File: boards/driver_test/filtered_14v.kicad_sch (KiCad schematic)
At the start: 3 parts

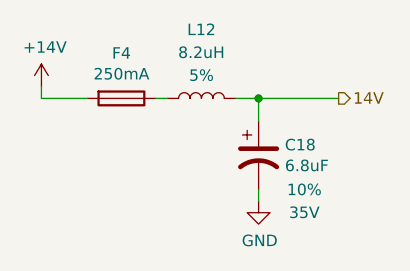
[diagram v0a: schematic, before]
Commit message: Driver: some high-level board rearrangement and addition of 3d models
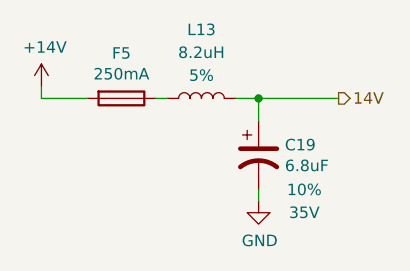
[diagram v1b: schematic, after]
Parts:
- renumbered C18 to C19, F4 to F5, L12 to L13
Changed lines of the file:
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@@
   (symbol (lib_id "Device:Fuse") (at 125.73 96.52 270)
     (in_bom yes) (on_board yes)
-    (property "Reference" "F4" (id 0) (at 125.73 91.5162 90))
+    (property "Reference" "F5" (id 0) (at 125.73 91.5162 90))
     (property "Value" "250mA" (id 1) (at 125.73 93.8276 90))
     (property "Footprint" "Fuse:Fuse_0603_1608Metric" (id 2) (at 125.73 94.742 90)
@@
   (symbol (lib_id "Device:L") (at 134.62 96.52 90)
     (in_bom yes) (on_board yes)
-    (property "Reference" "L12" (id 0) (at 134.62 88.9 90))
+    (property "Reference" "L13" (id 0) (at 134.62 88.9 90))
     (property "Value" "8.2uH" (id 1) (at 134.62 91.44 90))
     (property "Footprint" "Inductor_SMD:L_1812_4532Metric" (id 2) (at 134.62 96.52 0)
@@
   (symbol (lib_id "lachesis:+14V") (at 116.84 95.25 0)
     (in_bom yes) (on_board yes)
-    (property "Reference" "#PWR057" (id 0) (at 116.84 99.06 0)
+    (property "Reference" "#PWR061" (id 0) (at 116.84 99.06 0)
       (effects (font (size 1.27 1.27)) hide)
     )
@@
   (symbol (lib_id "power:GND") (at 140.97 107.95 0)
     (in_bom yes) (on_board yes)
-    (property "Reference" "#PWR058" (id 0) (at 140.97 114.3 0)
+    (property "Reference" "#PWR062" (id 0) (at 140.97 114.3 0)
       (effects (font (size 1.27 1.27)) hide)
     )
@@
   (symbol (lib_id "Device:C_Polarized_US") (at 140.97 102.87 0)
     (in_bom yes) (on_board yes)
-    (property "Reference" "C18" (id 0) (at 143.891 101.7016 0)
+    (property "Reference" "C19" (id 0) (at 143.891 101.7016 0)
       (effects (font (size 1.27 1.27)) (justify left))
     )

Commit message: Driver test: completed much of the preliminary layout.
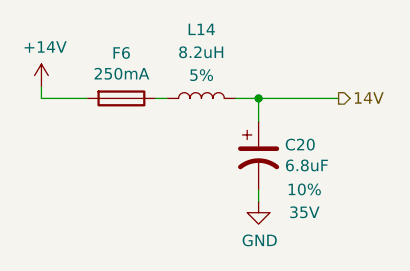
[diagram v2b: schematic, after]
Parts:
- renumbered C19 to C20, F5 to F6, L13 to L14
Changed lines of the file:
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@@
   (symbol (lib_id "Device:Fuse") (at 125.73 96.52 270)
     (in_bom yes) (on_board yes)
-    (property "Reference" "F5" (id 0) (at 125.73 91.5162 90))
+    (property "Reference" "F6" (id 0) (at 125.73 91.5162 90))
     (property "Value" "250mA" (id 1) (at 125.73 93.8276 90))
     (property "Footprint" "Fuse:Fuse_0603_1608Metric" (id 2) (at 125.73 94.742 90)
@@
   (symbol (lib_id "Device:L") (at 134.62 96.52 90)
     (in_bom yes) (on_board yes)
-    (property "Reference" "L13" (id 0) (at 134.62 88.9 90))
+    (property "Reference" "L14" (id 0) (at 134.62 88.9 90))
     (property "Value" "8.2uH" (id 1) (at 134.62 91.44 90))
     (property "Footprint" "Inductor_SMD:L_1812_4532Metric" (id 2) (at 134.62 96.52 0)
@@
   (symbol (lib_id "Device:C_Polarized_US") (at 140.97 102.87 0)
     (in_bom yes) (on_board yes)
-    (property "Reference" "C19" (id 0) (at 143.891 101.7016 0)
+    (property "Reference" "C20" (id 0) (at 143.891 101.7016 0)
       (effects (font (size 1.27 1.27)) (justify left))
     )

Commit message: Driver test: finished up board layout
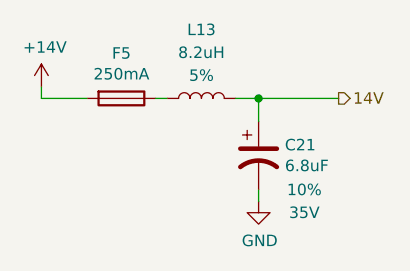
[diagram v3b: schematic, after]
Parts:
- renumbered C20 to C21, F6 to F5, L14 to L13
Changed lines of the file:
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@@
   (symbol (lib_id "Device:Fuse") (at 125.73 96.52 270)
     (in_bom yes) (on_board yes)
-    (property "Reference" "F6" (id 0) (at 125.73 91.5162 90))
+    (property "Reference" "F5" (id 0) (at 125.73 91.5162 90))
     (property "Value" "250mA" (id 1) (at 125.73 93.8276 90))
     (property "Footprint" "Fuse:Fuse_0603_1608Metric" (id 2) (at 125.73 94.742 90)
@@
   (symbol (lib_id "Device:L") (at 134.62 96.52 90)
     (in_bom yes) (on_board yes)
-    (property "Reference" "L14" (id 0) (at 134.62 88.9 90))
+    (property "Reference" "L13" (id 0) (at 134.62 88.9 90))
     (property "Value" "8.2uH" (id 1) (at 134.62 91.44 90))
     (property "Footprint" "Inductor_SMD:L_1812_4532Metric" (id 2) (at 134.62 96.52 0)
@@
   (symbol (lib_id "lachesis:+14V") (at 116.84 95.25 0)
     (in_bom yes) (on_board yes)
-    (property "Reference" "#PWR061" (id 0) (at 116.84 99.06 0)
+    (property "Reference" "#PWR065" (id 0) (at 116.84 99.06 0)
       (effects (font (size 1.27 1.27)) hide)
     )
@@
   (symbol (lib_id "power:GND") (at 140.97 107.95 0)
     (in_bom yes) (on_board yes)
-    (property "Reference" "#PWR062" (id 0) (at 140.97 114.3 0)
+    (property "Reference" "#PWR066" (id 0) (at 140.97 114.3 0)
       (effects (font (size 1.27 1.27)) hide)
     )
@@
   (symbol (lib_id "Device:C_Polarized_US") (at 140.97 102.87 0)
     (in_bom yes) (on_board yes)
-    (property "Reference" "C20" (id 0) (at 143.891 101.7016 0)
+    (property "Reference" "C21" (id 0) (at 143.891 101.7016 0)
       (effects (font (size 1.27 1.27)) (justify left))
     )

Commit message: Driver test: some minor component value changes
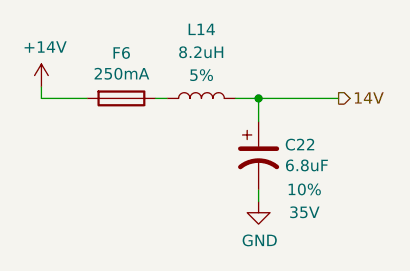
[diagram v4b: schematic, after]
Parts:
- renumbered C21 to C22, F5 to F6, L13 to L14
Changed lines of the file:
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@@
   (symbol (lib_id "Device:Fuse") (at 125.73 96.52 270)
     (in_bom yes) (on_board yes)
-    (property "Reference" "F5" (id 0) (at 125.73 91.5162 90))
+    (property "Reference" "F6" (id 0) (at 125.73 91.5162 90))
     (property "Value" "250mA" (id 1) (at 125.73 93.8276 90))
     (property "Footprint" "Fuse:Fuse_0603_1608Metric" (id 2) (at 125.73 94.742 90)
@@
   (symbol (lib_id "Device:L") (at 134.62 96.52 90)
     (in_bom yes) (on_board yes)
-    (property "Reference" "L13" (id 0) (at 134.62 88.9 90))
+    (property "Reference" "L14" (id 0) (at 134.62 88.9 90))
     (property "Value" "8.2uH" (id 1) (at 134.62 91.44 90))
     (property "Footprint" "Inductor_SMD:L_1812_4532Metric" (id 2) (at 134.62 96.52 0)
@@
   (symbol (lib_id "Device:C_Polarized_US") (at 140.97 102.87 0)
     (in_bom yes) (on_board yes)
-    (property "Reference" "C21" (id 0) (at 143.891 101.7016 0)
+    (property "Reference" "C22" (id 0) (at 143.891 101.7016 0)
       (effects (font (size 1.27 1.27)) (justify left))
     )

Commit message: Driver test: updated schematic with new coarse tuning resistance values for all 3 current driver types
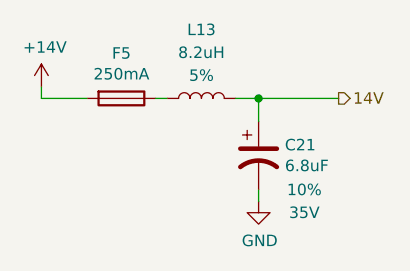
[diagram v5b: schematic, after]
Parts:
- renumbered C22 to C21, F6 to F5, L14 to L13
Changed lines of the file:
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@@
   (symbol (lib_id "Device:Fuse") (at 125.73 96.52 270)
     (in_bom yes) (on_board yes)
-    (property "Reference" "F6" (id 0) (at 125.73 91.5162 90))
+    (property "Reference" "F5" (id 0) (at 125.73 91.5162 90))
     (property "Value" "250mA" (id 1) (at 125.73 93.8276 90))
     (property "Footprint" "Fuse:Fuse_0603_1608Metric" (id 2) (at 125.73 94.742 90)
@@
   (symbol (lib_id "Device:L") (at 134.62 96.52 90)
     (in_bom yes) (on_board yes)
-    (property "Reference" "L14" (id 0) (at 134.62 88.9 90))
+    (property "Reference" "L13" (id 0) (at 134.62 88.9 90))
     (property "Value" "8.2uH" (id 1) (at 134.62 91.44 90))
     (property "Footprint" "Inductor_SMD:L_1812_4532Metric" (id 2) (at 134.62 96.52 0)
@@
   (symbol (lib_id "lachesis:+14V") (at 116.84 95.25 0)
     (in_bom yes) (on_board yes)
-    (property "Reference" "#PWR065" (id 0) (at 116.84 99.06 0)
+    (property "Reference" "#PWR063" (id 0) (at 116.84 99.06 0)
       (effects (font (size 1.27 1.27)) hide)
     )
@@
   (symbol (lib_id "power:GND") (at 140.97 107.95 0)
     (in_bom yes) (on_board yes)
-    (property "Reference" "#PWR066" (id 0) (at 140.97 114.3 0)
+    (property "Reference" "#PWR064" (id 0) (at 140.97 114.3 0)
       (effects (font (size 1.27 1.27)) hide)
     )
@@
   (symbol (lib_id "Device:C_Polarized_US") (at 140.97 102.87 0)
     (in_bom yes) (on_board yes)
-    (property "Reference" "C22" (id 0) (at 143.891 101.7016 0)
+    (property "Reference" "C21" (id 0) (at 143.891 101.7016 0)
       (effects (font (size 1.27 1.27)) (justify left))
     )
